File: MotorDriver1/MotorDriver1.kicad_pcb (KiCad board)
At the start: 4 copper layers, 72 x 76 mm, 79 parts, among them IC1 STM32C092RCT6, J1 GT-USB-7010ASV, J2 Conn_01x02, J3 Conn_01x02, Q1 IRLZ44NSTRLPBF, Q2 IRLZ44NSTRLPBF, Q3 IRLZ44NSTRLPBF, Q4 IRLZ44NSTRLPBF, SW1 K2-6639SP-C4SC-04, SW2 K2-6639SP-C4SC-04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

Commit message: Re-generated gerbers
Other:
- board text added: "WARNING: DO NOT USE ESP USB IF BATTERY IS ON"
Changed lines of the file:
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@@
 		(tags "capacitor")
 		(property "Reference" "C_A1"
-			(at 0 -1.16 270)
-			(layer "F.SilkS")
-			(effects
-				(font
-					(size 1 1)
-					(thickness 0.15)
+			(at 2.3779 0 90)
+			(layer "F.SilkS")
+			(effects
+				(font
+					(size 0.8 0.8)
+					(thickness 0.1)
 				)
 			)
@@
 		(tags "capacitor")
 		(property "Reference" "C_D1"
-			(at 0 -1.16 90)
-			(layer "F.SilkS")
-			(effects
-				(font
-					(size 1 1)
-					(thickness 0.15)
+			(at -2.2779 -0.1 90)
+			(layer "F.SilkS")
+			(effects
+				(font
+					(size 0.8 0.8)
+					(thickness 0.1)
 				)
 			)
@@
 	)
 	(gr_text "BOOT"
-		(at 168.5 97 0)
+		(at 170 97.75 0)
 		(layer "F.SilkS")
 		(effects
@@
 		)
 	)
+	(gr_text "WARNING:\nDO NOT USE ESP USB\nIF BATTERY IS ON"
+		(at 150.5 54.75 0)
+		(layer "F.SilkS")
+		(effects
+			(font
+				(size 0.9 0.9)
+				(thickness 0.1125)
+			)
+			(justify left bottom)
+		)
+	)

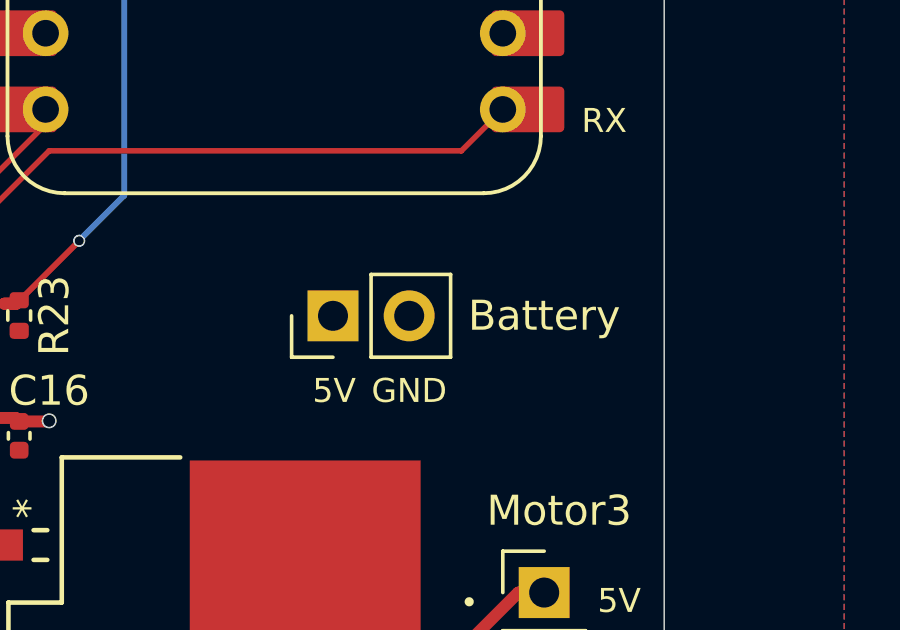
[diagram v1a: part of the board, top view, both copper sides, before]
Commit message: Added battery fuse
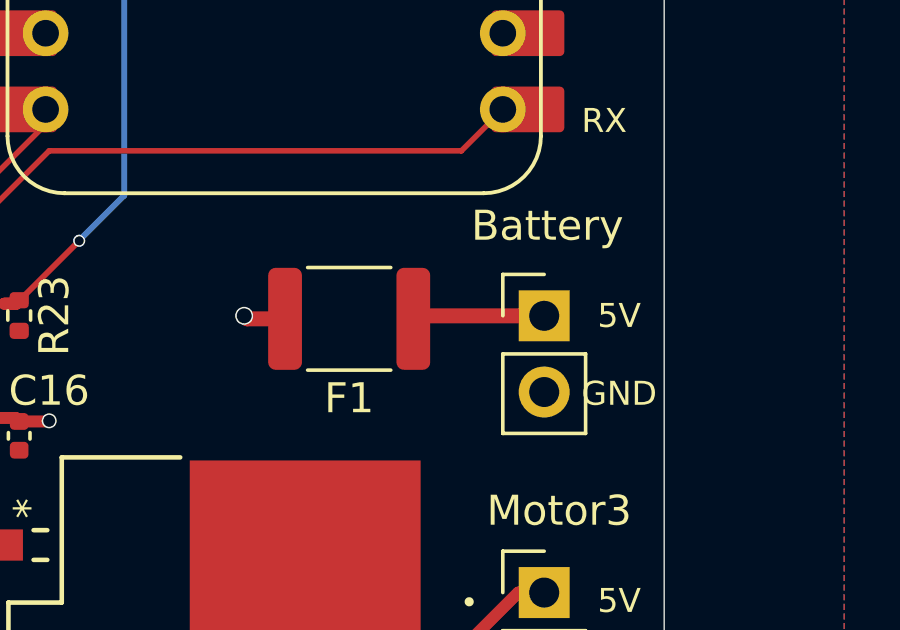
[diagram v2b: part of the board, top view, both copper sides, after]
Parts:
- added F1: MINISMDC260F/16-2, Fuse:Fuse_1812_4532Metric, F.Cu at (177.5, 78.1)
- moved VBAT1 7.04 mm to (184.0, 78.0), turned to 0 degrees
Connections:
- VBAT1 pad 1: 5V -> Net-(VBAT1-Pin_1)
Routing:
- net 5V: track 109.6 -> 94.7 mm, vias 4 -> 5
- net Net-(VBAT1-Pin_1): track 0.00 -> 4.40 mm

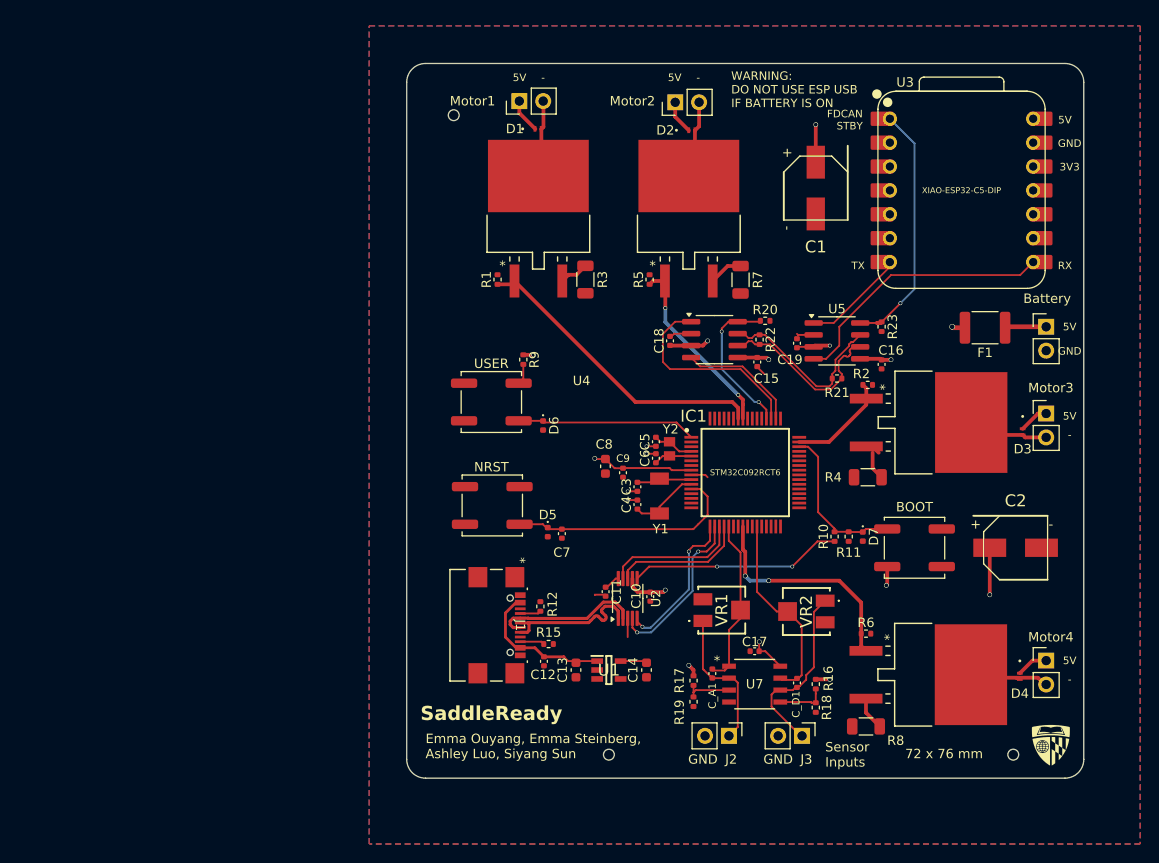
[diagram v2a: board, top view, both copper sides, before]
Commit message: added motors and sensors for 4 pad system
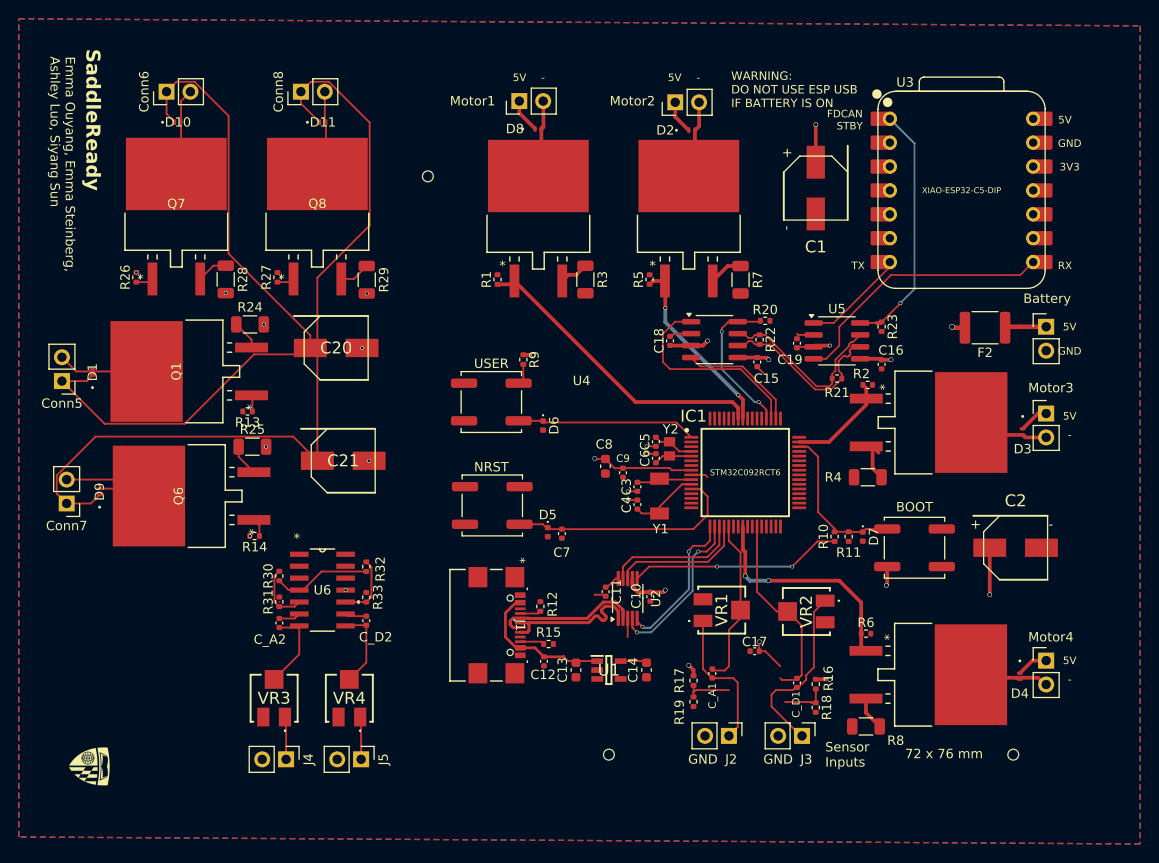
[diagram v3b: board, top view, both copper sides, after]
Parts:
- removed U7: LMV358AIDR, footprintLib:D8_TEX
- added C20: MAL214297108E3, footprintLib:CAPAE680X800N, F.Cu at (108.5, 80.2)
- added C21: MAL214297108E3, footprintLib:CAPAE680X800N, F.Cu at (109.2, 92.2)
- added C_A2: 47 nF, Capacitor_SMD:C_0402_1005Metric, F.Cu at (102.5, 109.5)
- added C_D2: 47 nF, Capacitor_SMD:C_0402_1005Metric, F.Cu at (111.7, 109.3)
- added Conn5: Motor5, Connector_PinHeader_2.54mm:PinHeader_1x02_P2.54mm_Vertical, F.Cu at (79.3, 83.8)
- added Conn6: Motor6, Connector_PinHeader_2.54mm:PinHeader_1x02_P2.54mm_Vertical, F.Cu at (90.5, 53.0)
- added Conn7: Motor7, Connector_PinHeader_2.54mm:PinHeader_1x02_P2.54mm_Vertical, F.Cu at (79.8, 96.8)
- added Conn8: Motor8, Connector_PinHeader_2.54mm:PinHeader_1x02_P2.54mm_Vertical, F.Cu at (104.8, 53.0)
- added D1: SM5819L2-TP, footprintLib:SDO_SM5819L2-TP_MCE, F.Cu at (82.6, 82.8)
- added D10: SM5819L2-TP, footprintLib:SDO_SM5819L2-TP_MCE, F.Cu at (91.7, 56.2)
- added D11: SM5819L2-TP, footprintLib:SDO_SM5819L2-TP_MCE, F.Cu at (107.1, 56.2)
- added D9: SM5819L2-TP, footprintLib:SDO_SM5819L2-TP_MCE, F.Cu at (83.3, 95.5)
- added J4: Conn_01x02, Connector_PinHeader_2.54mm:PinHeader_1x02_P2.54mm_Vertical, F.Cu at (103.2, 124.0)
- added J5: Conn_01x02, Connector_PinHeader_2.54mm:PinHeader_1x02_P2.54mm_Vertical, F.Cu at (111.2, 124.0)
- added Q1: IRLZ44NSTRLPBF, footprintLib:NMOSGDS_D2PAK_INF, F.Cu at (91.5, 82.8)
- added Q6: IRLZ44NSTRLPBF, footprintLib:NMOSGDS_D2PAK_INF, F.Cu at (91.8, 96.0)
- added Q7: IRLZ44NSTRLPBF, footprintLib:NMOSGDS_D2PAK_INF, F.Cu at (91.5, 64.9)
- added Q8: IRLZ44NSTRLPBF, footprintLib:NMOSGDS_D2PAK_INF, F.Cu at (106.5, 64.9)
- added R13: 10k, Resistor_SMD:R_0402_1005Metric, F.Cu at (99.1, 87.0)
- added R14: 10k, Resistor_SMD:R_0402_1005Metric, F.Cu at (99.8, 100.2)
- added R24: 1, Resistor_SMD:R_1206_3216Metric, F.Cu at (99.3, 77.8)
- added R25: 1, Resistor_SMD:R_1206_3216Metric, F.Cu at (99.6, 90.8)
- added R26: 10k, Resistor_SMD:R_0402_1005Metric, F.Cu at (87.2, 72.7)
- added R27: 10k, Resistor_SMD:R_0402_1005Metric, F.Cu at (102.2, 72.7)
- added R28: 1, Resistor_SMD:R_1206_3216Metric, F.Cu at (96.8, 73.0)
- added R29: 1, Resistor_SMD:R_1206_3216Metric, F.Cu at (111.8, 73.0)
- added R30: 10k, Resistor_SMD:R_0402_1005Metric, F.Cu at (102.5, 104.5)
- added R31: 1.8k, Resistor_SMD:R_0402_1005Metric, F.Cu at (102.5, 107.3)
- added R32: 10k, Resistor_SMD:R_0402_1005Metric, F.Cu at (111.7, 103.5)
- added R33: 1.8k, Resistor_SMD:R_0402_1005Metric, F.Cu at (111.7, 106.8)
- added U6: LM324DR, footprintLib:D14, F.Cu at (107.0, 106.0)
- added VR3: TS53YJ105MR10, footprintLib:TS53YJ105MR10, F.Cu at (101.9, 117.5)
- added VR4: TS53YJ105MR10, footprintLib:TS53YJ105MR10, F.Cu at (109.9, 117.5)
- moved G*** 102.3 mm to (82.2, 124.8), turned to -90 degrees
- moved H1 7.06 mm to (118.2, 62.0)
- renumbered D1 to D8, F1 to F2, Q1 to Q5
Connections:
- net /motorDriver/Motor1- renamed /motorDriver_Pads12/Motor1-
- net /motorDriver/Motor2- renamed /motorDriver_Pads12/Motor2-
- net /motorDriver/Motor3- renamed /motorDriver_Pads12/Motor3-
- net /motorDriver/Motor4- renamed /motorDriver_Pads12/Motor4-
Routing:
- net 5V: track 94.7 -> 259.9 mm
- net /motorDriver_Pads34/Motor7-: track 0.00 -> 15.1 mm
- net 3V3: track 31.8 -> 42.3 mm
- net /motorDriver_Pads34/Motor5-: track 0.00 -> 9.63 mm
- net /motorDriver_Pads34/Motor6-: track 0.00 -> 9.37 mm
- net /motorDriver_Pads34/Motor8-: track 0.00 -> 9.18 mm
- net SensorBOut: track 0.00 -> 8.99 mm
- net SensorCOut: track 0.00 -> 8.75 mm
- net SensorC_0.5V: track 0.00 -> 6.93 mm
- net SensorBIn: track 0.00 -> 6.87 mm
- net SensorCIn: track 0.00 -> 6.84 mm
- net SensorB_0.5V: track 0.00 -> 6.54 mm
- net Net-(Q6-S): track 0.00 -> 3.38 mm
- net Net-(Q7-S): track 0.00 -> 3.29 mm
- net Net-(Q8-S): track 0.00 -> 3.28 mm
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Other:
- board outline removed
